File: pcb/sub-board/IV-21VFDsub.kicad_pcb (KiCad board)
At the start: 2 copper layers, 36.6 x 28.9 mm, 2 parts, among them X1 TSW-110-07-G-D

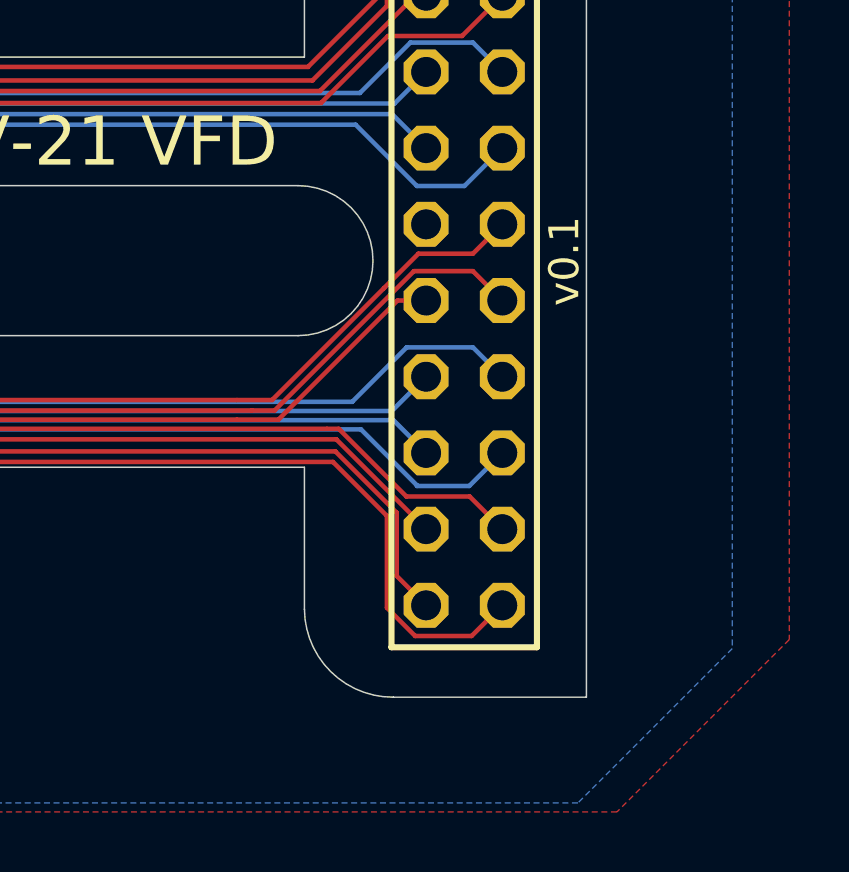
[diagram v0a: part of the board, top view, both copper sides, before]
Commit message: Fixed rounded corner to match other rounded corner.
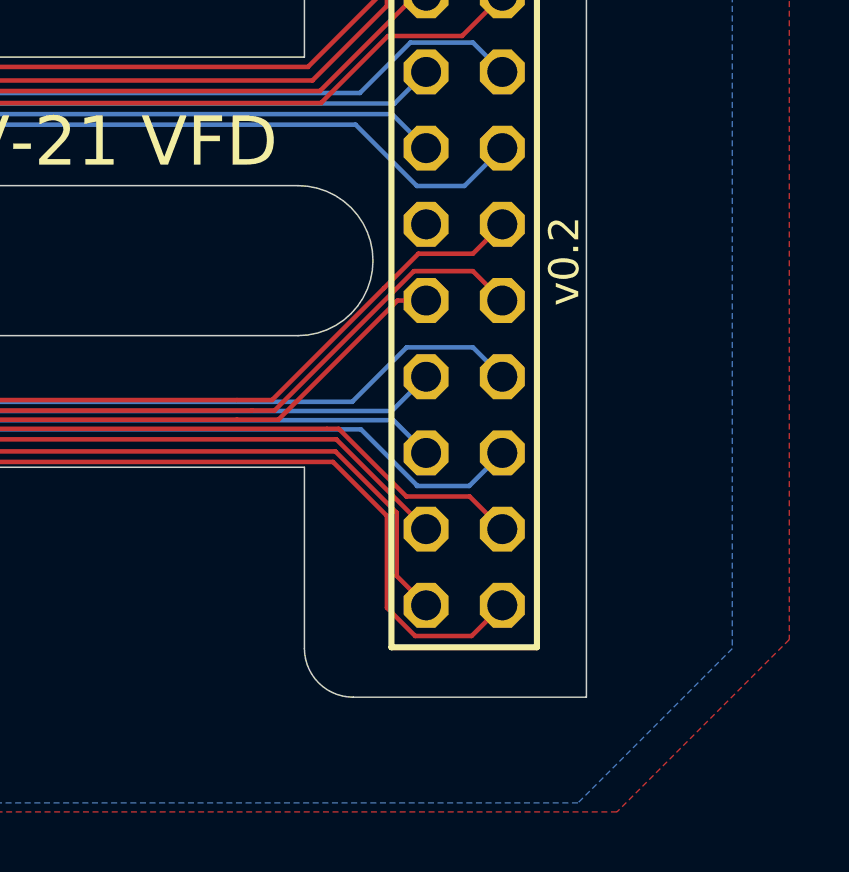
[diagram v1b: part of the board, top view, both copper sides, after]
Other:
- outline, holes or cut-outs redrawn
- board text added: "v0.2"
- board text removed: "v0.1"
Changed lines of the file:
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@@
 		(embedded_fonts no)
 	)
-	(gr_arc
-		(start 161.216713 119.5396)
-		(mid 159.125167 118.685762)
-		(end 158.249976 116.603061)
-		(stroke
-			(width 0.05)
-			(type solid)
-		)
-		(layer "Edge.Cuts")
-	)
 	(gr_line
-		(start 158.25 116.607246)
+		(start 158.25 117.915207)
 		(end 158.25 111.87593)
 		(stroke
@@
 	)
 	(gr_line
-		(start 161.216713 119.5396)
+		(start 159.874638 119.539845)
 		(end 167.65 119.5396)
 		(stroke
@@
 		(layer "Edge.Cuts")
 	)
+	(gr_arc
+		(start 159.874638 119.539845)
+		(mid 158.725845 119.064)
+		(end 158.25 117.915207)
+		(stroke
+			(width 0.05)
+			(type solid)
+		)
+		(layer "Edge.Cuts")
+	)
 	(gr_line
 		(start 167.65 90.6)
@@
 		)
 	)
-	(gr_text "v0.1"
+	(gr_text "v0.2"
 		(at 167.5 106.5 90)
 		(layer "F.SilkS")

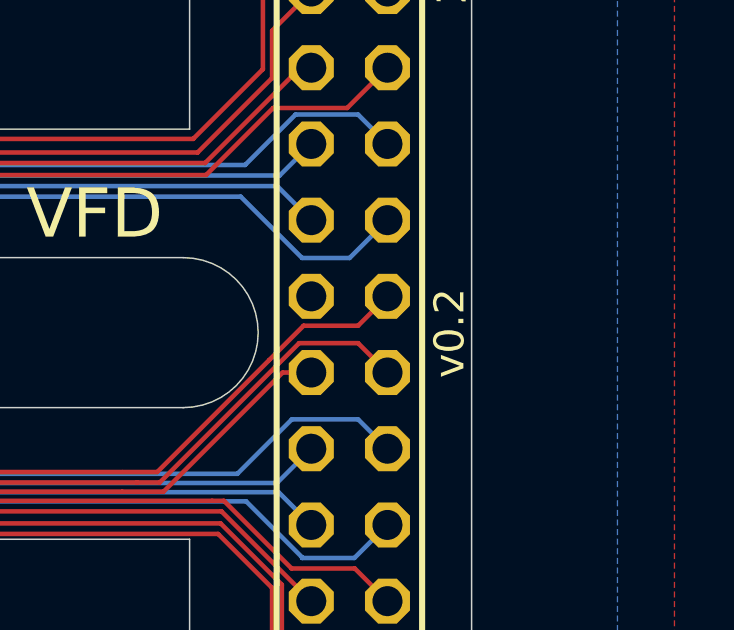
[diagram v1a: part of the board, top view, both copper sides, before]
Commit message: Update silkscreen labels to say v0.3
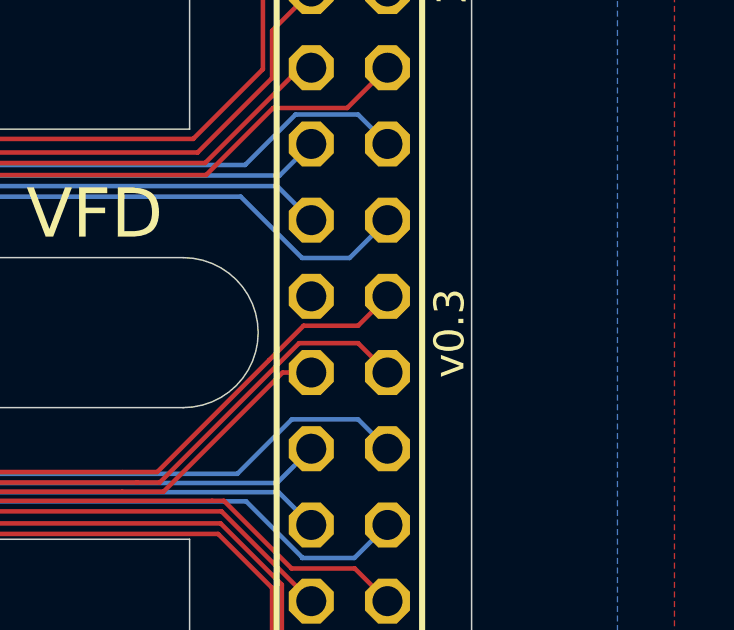
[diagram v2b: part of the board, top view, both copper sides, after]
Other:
- board text added: "v0.3"
- board text removed: "v0.2"
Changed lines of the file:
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@@
 		)
 	)
-	(gr_text "v0.2"
+	(gr_text "v0.3"
 		(at 167.5 106.5 90)
 		(layer "F.SilkS")
